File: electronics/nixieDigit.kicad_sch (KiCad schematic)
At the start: 2 parts, among them U8 KAQY214ATLD

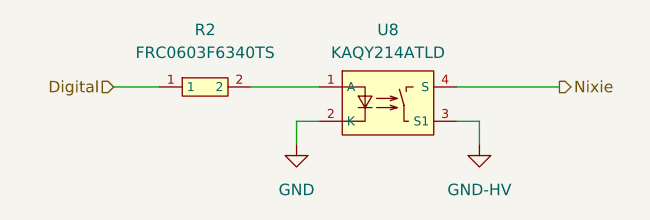
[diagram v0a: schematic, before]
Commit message: update resistor
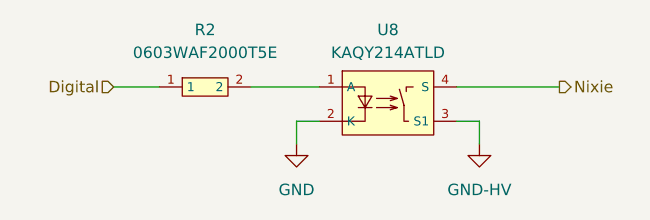
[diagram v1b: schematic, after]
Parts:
- R2: value FRC0603F6340TS -> 0603WAF2000T5E; LCSC C23138 -> C8218
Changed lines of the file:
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@@
 			)
 		)
-		(property "Value" "FRC0603F6340TS"
+		(property "Value" "0603WAF2000T5E"
 			(at 120.65 82.55 0)
 			(effects
@@
 			)
 		)
-		(property "LCSC" "C23138"
+		(property "LCSC" "C8218"
 			(at 120.65 86.36 0)
 			(effects

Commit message: update resistor, update voltages
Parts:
- R2: symbol symbols:FRC0603F6340TS -> symbols:0603WAF2000T5E
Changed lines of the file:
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@@
 	)
 	(symbol
-		(lib_id "symbols:FRC0603F6340TS")
+		(lib_id "symbols:0603WAF2000T5E")
 		(at 120.65 86.36 0)
 		(unit 1)
